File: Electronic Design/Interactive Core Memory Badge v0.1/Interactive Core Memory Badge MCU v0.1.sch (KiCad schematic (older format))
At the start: 1 part, among them U1 Teensy-LC

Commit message: Schematic Complete
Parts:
- added R28, R31, R34: 1K5, Resistor_SMD:R_0805_2012Metric, symbol Device:R
- added R29, R32: 1K8, Resistor_SMD:R_0805_2012Metric, symbol Device:R
- added R30, R33: 22, Resistor_SMD:R_0805_2012Metric, symbol Device:R
- added R35, R36, R37: 10k, Resistor_SMD:R_0805_2012Metric, symbol Device:R
- added R38, R39: 4K7, Resistor_SMD:R_0805_2012Metric, symbol Device:R
- added U3: LM393, Digikey:SOIC-8_W3.9mm, symbol Comparator:LM393
- renumbered U1 to U2
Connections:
- net -BATT: now also U2.32 (GND), R37.2; no longer U2.17 (GND)
- net GNDD: now reaches U2.1 (GND)
- net GNDD: now also U2.17 (GND), R31.2, R34.2, U3.4 (V-)
- net Q4N: now reaches U2.10 (8_TX3_MISO0)
- net Q5P: now reaches U2.11 (9_RX2_PWM)
- net Q5N: now reaches U2.12 (10_TX2_CS0_PWM)
- net Q6P: now reaches U2.13 (11_MOSI0)
- net Q6N: now reaches U2.14 (12_MISO0)
- net AVAILABLE: now reaches U2.19 (26_A12/DAC)
- net SENSE_PULSE: now reaches U2.2 (0_RX1_MOSI1_Touch)
- net SENSE_PULSE: now also R35.2, U3.1, U3.7
- net Q7P: now reaches U2.20 (13_LED_SCK0)
- net Q7N: now reaches U2.21 (14_A0_SCK0)
- net Q8P: now reaches U2.22 (15_A1_Touch)
- net Q8N: now reaches U2.23 (16_A2_SCL0_PWM_Touch)
- net Q9P: now reaches U2.24 (17_A3_SDA0_PWM_Touch)
- net I2C_DATA: now reaches U2.25 (18_A4_SDA0_Touch)
- net I2C_DATA: now also R38.2
- net I2C_CLOCK: now reaches U2.26 (19_A5_SCL0_Touch)
- net I2C_CLOCK: now also R39.2
- net Q9N: now reaches U2.27 (20_A6_SCK1_PWM_TX3)
- net Q10P: now reaches U2.28 (21_A7_MOSI1_RX1)
- net Q10N: now reaches U2.29 (22_A8_SCL1_PWM_Touch)
- net WRITE_ENABLE: now reaches U2.30 (23_A9_SDA1_PWM_Touch)
- net +3V3: now reaches U2.31 (3.3V_max100mA)
- net +3V3: now also U2.35 (AREF), R29.1, R32.1, R35.1, R38.1, R39.1, U3.8 (V+)
- net V+USB: now reaches U2.34 (VUSB)
- net at U2.36 (24_A10): now also R36.2, R37.1
- net REED_SWITCH: now reaches U2.37 (25_A11)
- net Q2P: now reaches U2.5 (3_RX1_PWM_Touch)
- net Q2N: now reaches U2.6 (4_TX1_PWM_Touch)
- net Q3P: now reaches U2.7 (5_TX1_MISO1)
- net Q3N: now reaches U2.8 (6_RX3_CS1_PWM)
- net Q4P: now reaches U2.9 (7_RX3_MOSI0)
- net +BATT renamed +VSW
- net +VSW: now also R36.1
- new net: R29.2, R30.1, U3.5 (+)
- new net: R32.2, R33.1, U3.2 (-)
- new net SENSE1: R28.1, R33.2, R34.1, U3.6 (_)
- new net SENSE2: R28.2, R30.2, R31.1, U3.3 (+)
- no-connect marks 0 -> 5
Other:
- note added: "Battery Voltage Monitor\nAnalog reads 1/2 battery voltage"
- note added: "SENSE SIGNAL PROCESSING"
- note added: "TO DO EXPANSION FEMALE .100” HEADER:\nAll power and logic"
- note added: "Teensy LC has incoming USB\npower/programming on board.\n\nUSB V+ bridge cut and routes ONLY\nto the LiPo charger module.\n\nLiPo must be connected for whole\nsystem to work."
- note added: "Use +3V3 for low power accessories:\nReed switch, hall sensors, sense circuit, expansion bus, …"
- moved on the sheet: U2

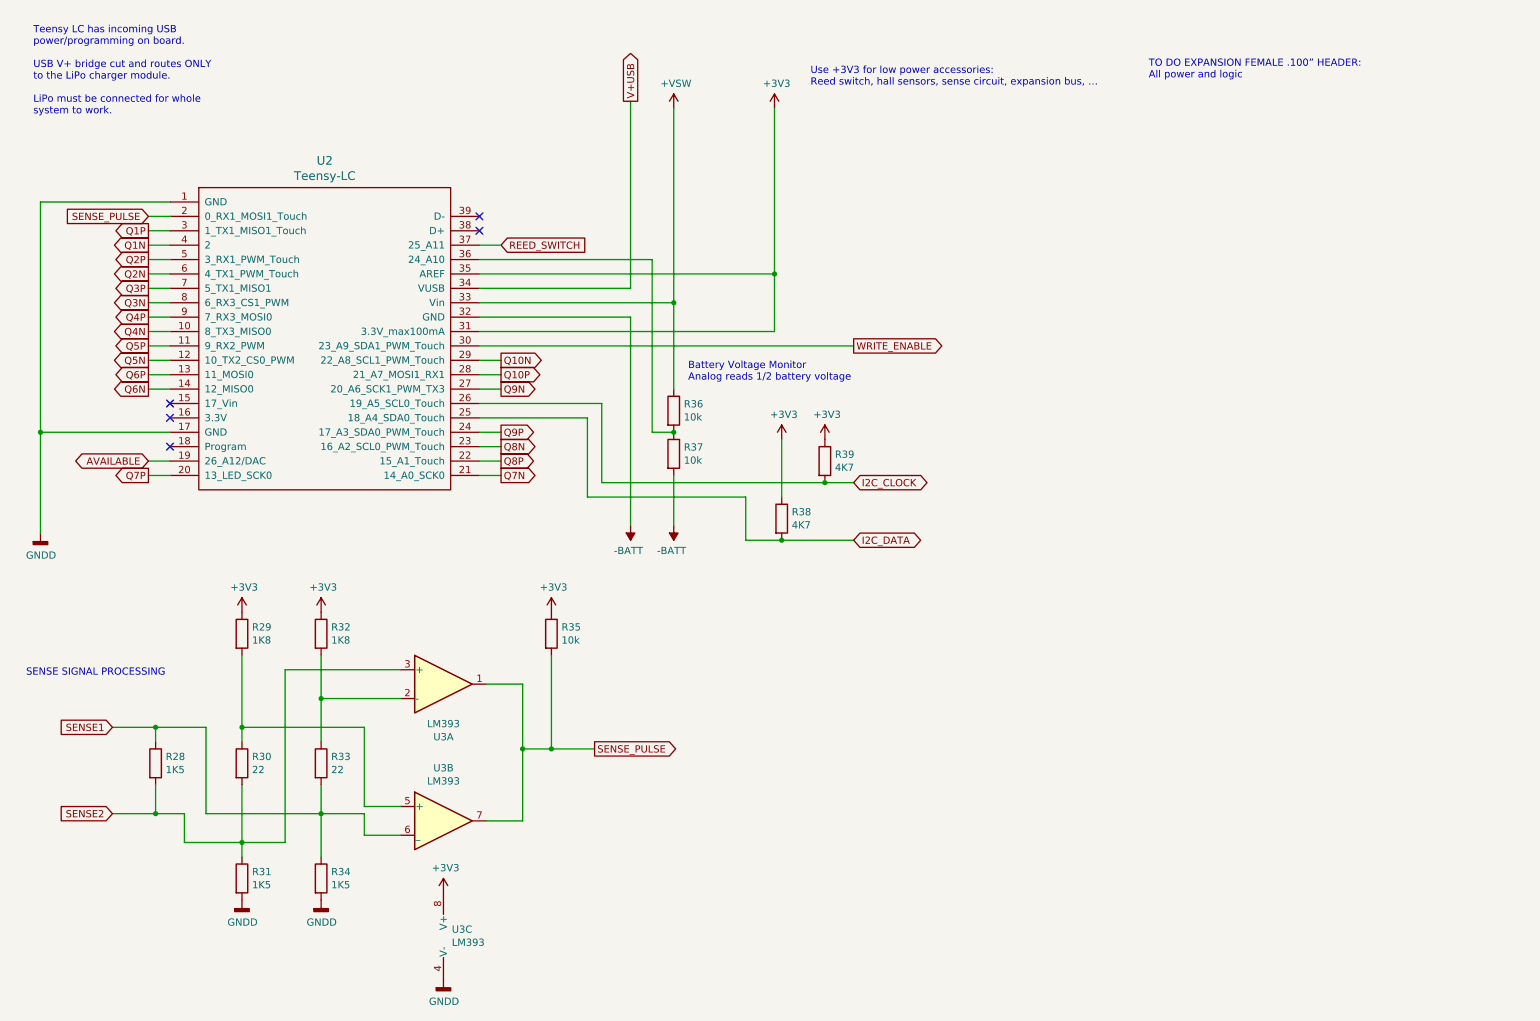
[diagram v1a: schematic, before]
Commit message: Layout 75% complete for V0.1
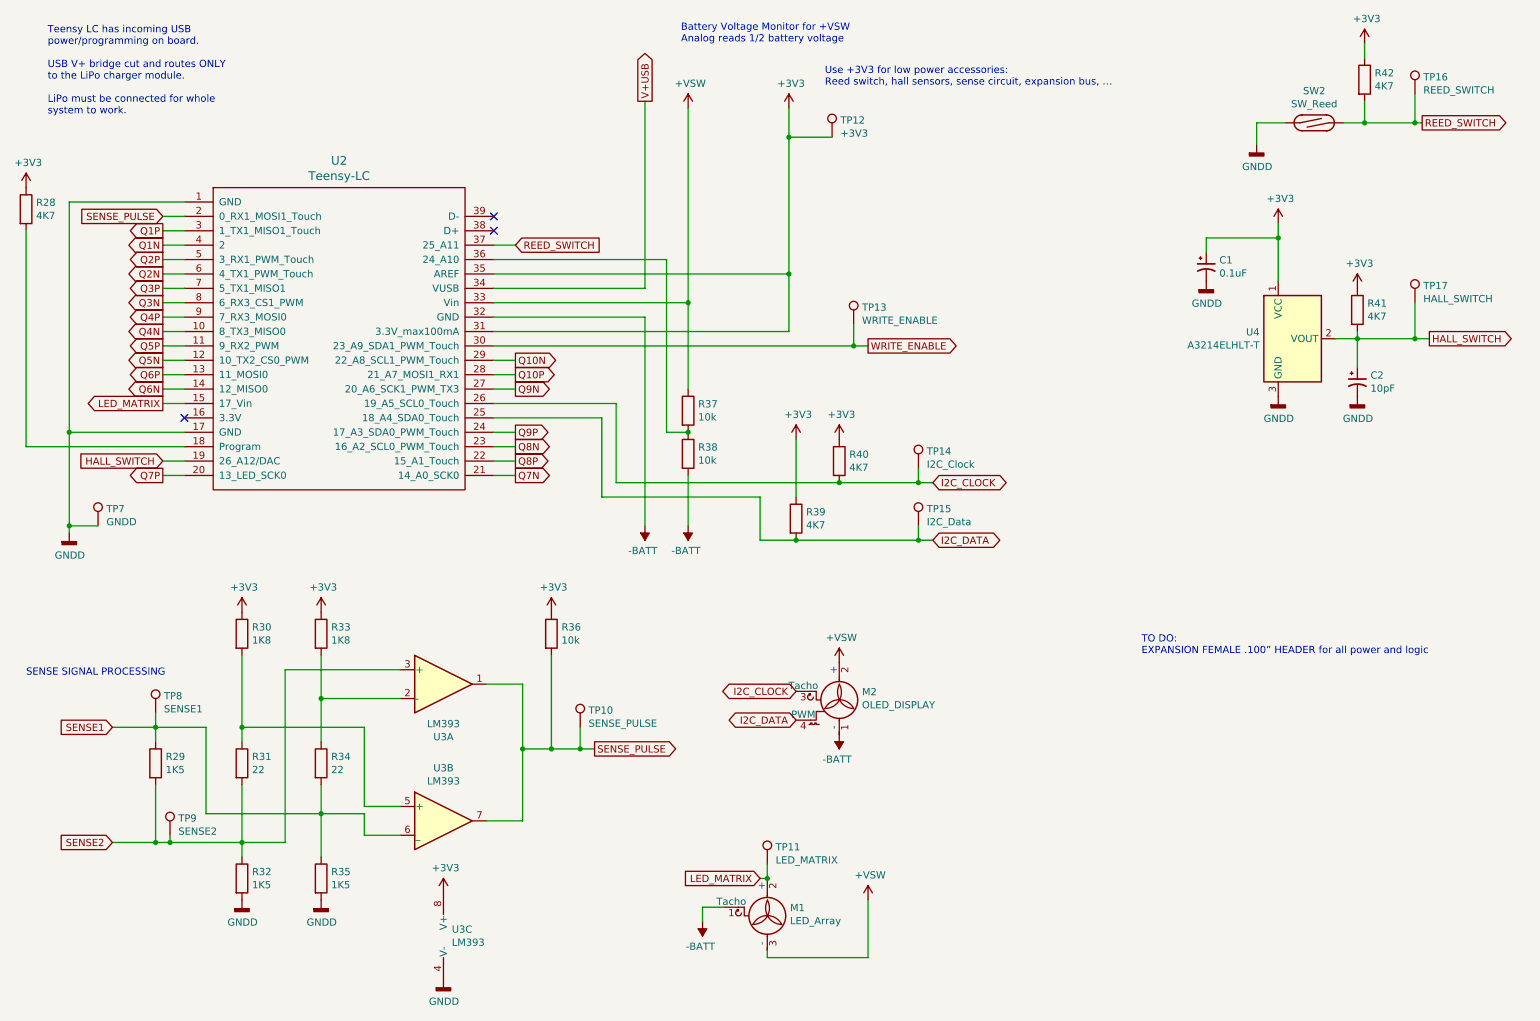
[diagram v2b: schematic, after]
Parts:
- added C1: 0.1uF, Capacitor_SMD:C_0805_2012Metric, symbol Device:CP1_Small
- added C2: 10pF, Capacitor_SMD:C_0805_2012Metric, symbol Device:CP1_Small
- added M1: LED_Array, Connector:FanPinHeader_1x03_P2.54mm_Vertical, symbol Motor:Fan_3pin
- added M2: OLED_DISPLAY, Connector:FanPinHeader_1x04_P2.54mm_Vertical, symbol Motor:Fan_4pin
- added R28, R41, R42: 4K7, Resistor_SMD:R_0805_2012Metric, symbol Device:R
- added SW2: SW_Reed, Button_Switch_SMD:SW_SPST_REED_CT10-XXXX-G1, symbol Switch:SW_Reed
- added TP10: SENSE_PULSE, TestPoint:TestPoint_Keystone_5000-5004_Miniature, symbol Connector:TestPoint
- added TP11: LED_MATRIX, TestPoint:TestPoint_Keystone_5000-5004_Miniature, symbol Connector:TestPoint
- added TP12: +3V3, TestPoint:TestPoint_Keystone_5000-5004_Miniature, symbol Connector:TestPoint
- added TP13: WRITE_ENABLE, TestPoint:TestPoint_Keystone_5000-5004_Miniature, symbol Connector:TestPoint
- added TP14: I2C_Clock, TestPoint:TestPoint_Keystone_5000-5004_Miniature, symbol Connector:TestPoint
- added TP15: I2C_Data, TestPoint:TestPoint_Keystone_5000-5004_Miniature, symbol Connector:TestPoint
- added TP16: REED_SWITCH, TestPoint:TestPoint_Keystone_5000-5004_Miniature, symbol Connector:TestPoint
- added TP17: HALL_SWITCH, TestPoint:TestPoint_Keystone_5000-5004_Miniature, symbol Connector:TestPoint
- added TP7: GNDD, TestPoint:TestPoint_Keystone_5000-5004_Miniature, symbol Connector:TestPoint
- added TP8: SENSE1, TestPoint:TestPoint_Keystone_5000-5004_Miniature, symbol Connector:TestPoint
- added TP9: SENSE2, TestPoint:TestPoint_Keystone_5000-5004_Miniature, symbol Connector:TestPoint
- added U4: A3214ELHLT-T, Package_TO_SOT_SMD:SOT-23W_Handsoldering, symbol Sensor_Magnetic:A3214ELHLT-T
- renumbered R28 to R29, R29 to R30, R30 to R31, R31 to R32, R32 to R33, R33 to R34, R34 to R35, R35 to R36, R36 to R37, R37 to R38, R38 to R39, R39 to R40
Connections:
- net +3V3: now also C1.1, R28.1, R41.1, R42.1, TP12.1, U4.1 (VCC)
- net +VSW: now also M1.3 (-), M2.2 (+)
- net -BATT: now also M1.1 (Tacho), M2.1 (-)
- net GNDD: now also C1.2, C2.2, SW2.1, TP7.1, U4.3 (GND)
- net I2C_CLOCK: now also M2.3 (Tacho), TP14.1
- net I2C_DATA: now also M2.4 (PWM), TP15.1
- net REED_SWITCH: now also R42.2, SW2.2, TP16.1
- net SENSE1: now also TP8.1
- net SENSE2: now also TP9.1
- net SENSE_PULSE: now also TP10.1
- net WRITE_ENABLE: now also TP13.1
- net LED_MATRIX: now reaches U2.15 (17_Vin)
- net LED_MATRIX: now also M1.2 (+), TP11.1
- net at U2.18 (Program): now also R28.2
- net AVAILABLE renamed HALL_SWITCH
- net HALL_SWITCH: now also C2.1, R41.2, TP17.1, U4.2 (VOUT)
- no-connect marks 5 -> 3
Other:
- note added: "Battery Voltage Monitor for +VSW\nAnalog reads 1/2 battery voltage"
- note added: "TO DO:\nEXPANSION FEMALE .100” HEADER for all power and logic"
- note removed: "Battery Voltage Monitor\nAnalog reads 1/2 battery voltage"
- note removed: "TO DO EXPANSION FEMALE .100” HEADER:\nAll power and logic"
- moved on the sheet: R37, R38, R39, R40, U2

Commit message: Prototype release V0.1
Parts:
- H1: renamed from M1; footprint Connector:FanPinHeader_1x03_P2.54mm_Vertical -> Core_Memory_8x8_Array:LED_Matrix_Header_3pin
- H2: renamed from M2; footprint Connector:FanPinHeader_1x04_P2.54mm_Vertical -> Core_Memory_8x8_Array:OLED_Header_4PIN
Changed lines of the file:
@@
 	1650 3350 1800 3350
 $Comp
-L Motor:Fan_3pin M1
+L Motor:Fan_3pin H1
 U 1 1 5D465797
 P 5850 6850
-F 0 "M1" H 6008 6846 50  0000 L CNN
+F 0 "H1" H 6008 6846 50  0000 L CNN
 F 1 "LED_Array" H 6008 6755 50  0000 L CNN
-F 2 "Connector:FanPinHeader_1x03_P2.54mm_Vertical" H 5850 6760 50  0001 C CNN
-F 3 "http://www.hardwarecanucks.com/forum/attachments/new-builds/16287d1330775095-help-chassis-power-fan-connectors-motherboard-asus_p8z68.jpg" H 5850 6760 50  0001 C CNN
+F 2 "Core_Memory_8x8_Array:LED_Matrix_Header_3pin" H 5850 6760 50  0001 C CNN
+F 3 "" H 5850 6760 50  0001 C CNN
 	1    5850 6850
 	1    0    0    -1
@@
 	9400 2200 9400 2100
 $Comp
-L Motor:Fan_4pin M2
+L Motor:Fan_4pin H2
 U 1 1 5D49F2EF
 P 6350 5450
-F 0 "M2" H 6508 5546 50  0000 L CNN
+F 0 "H2" H 6508 5546 50  0000 L CNN
 F 1 "OLED_DISPLAY" H 6508 5455 50  0000 L CNN
-F 2 "Connector:FanPinHeader_1x04_P2.54mm_Vertical" H 6350 5460 50  0001 C CNN
-F 3 "http://www.formfactors.org/developer%5Cspecs%5Crev1_2_public.pdf" H 6350 5460 50  0001 C CNN
+F 2 "Core_Memory_8x8_Array:OLED_Header_4PIN" H 6350 5460 50  0001 C CNN
+F 3 "" H 6350 5460 50  0001 C CNN
 	1    6350 5450
 	1    0    0    -1
